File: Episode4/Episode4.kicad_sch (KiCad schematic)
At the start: 8 parts, among them J1 5V DC

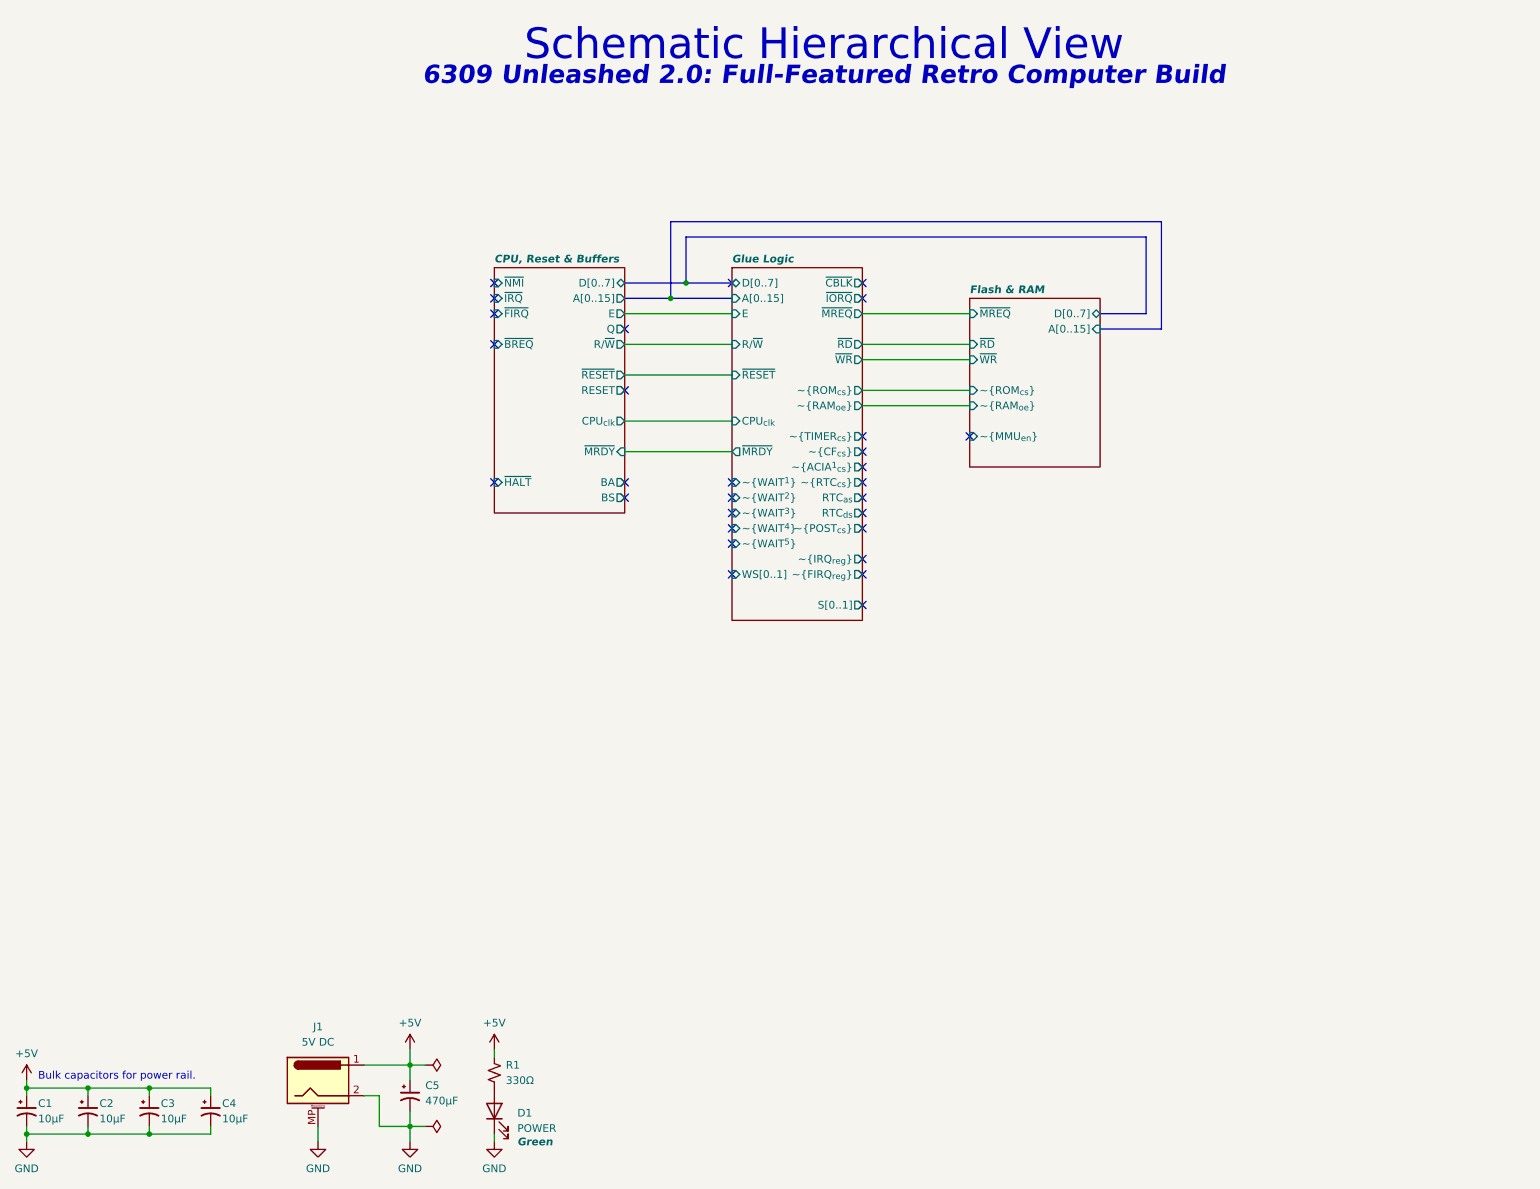
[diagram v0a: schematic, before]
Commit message: Project Update, change in strategy from breadboard to PCB
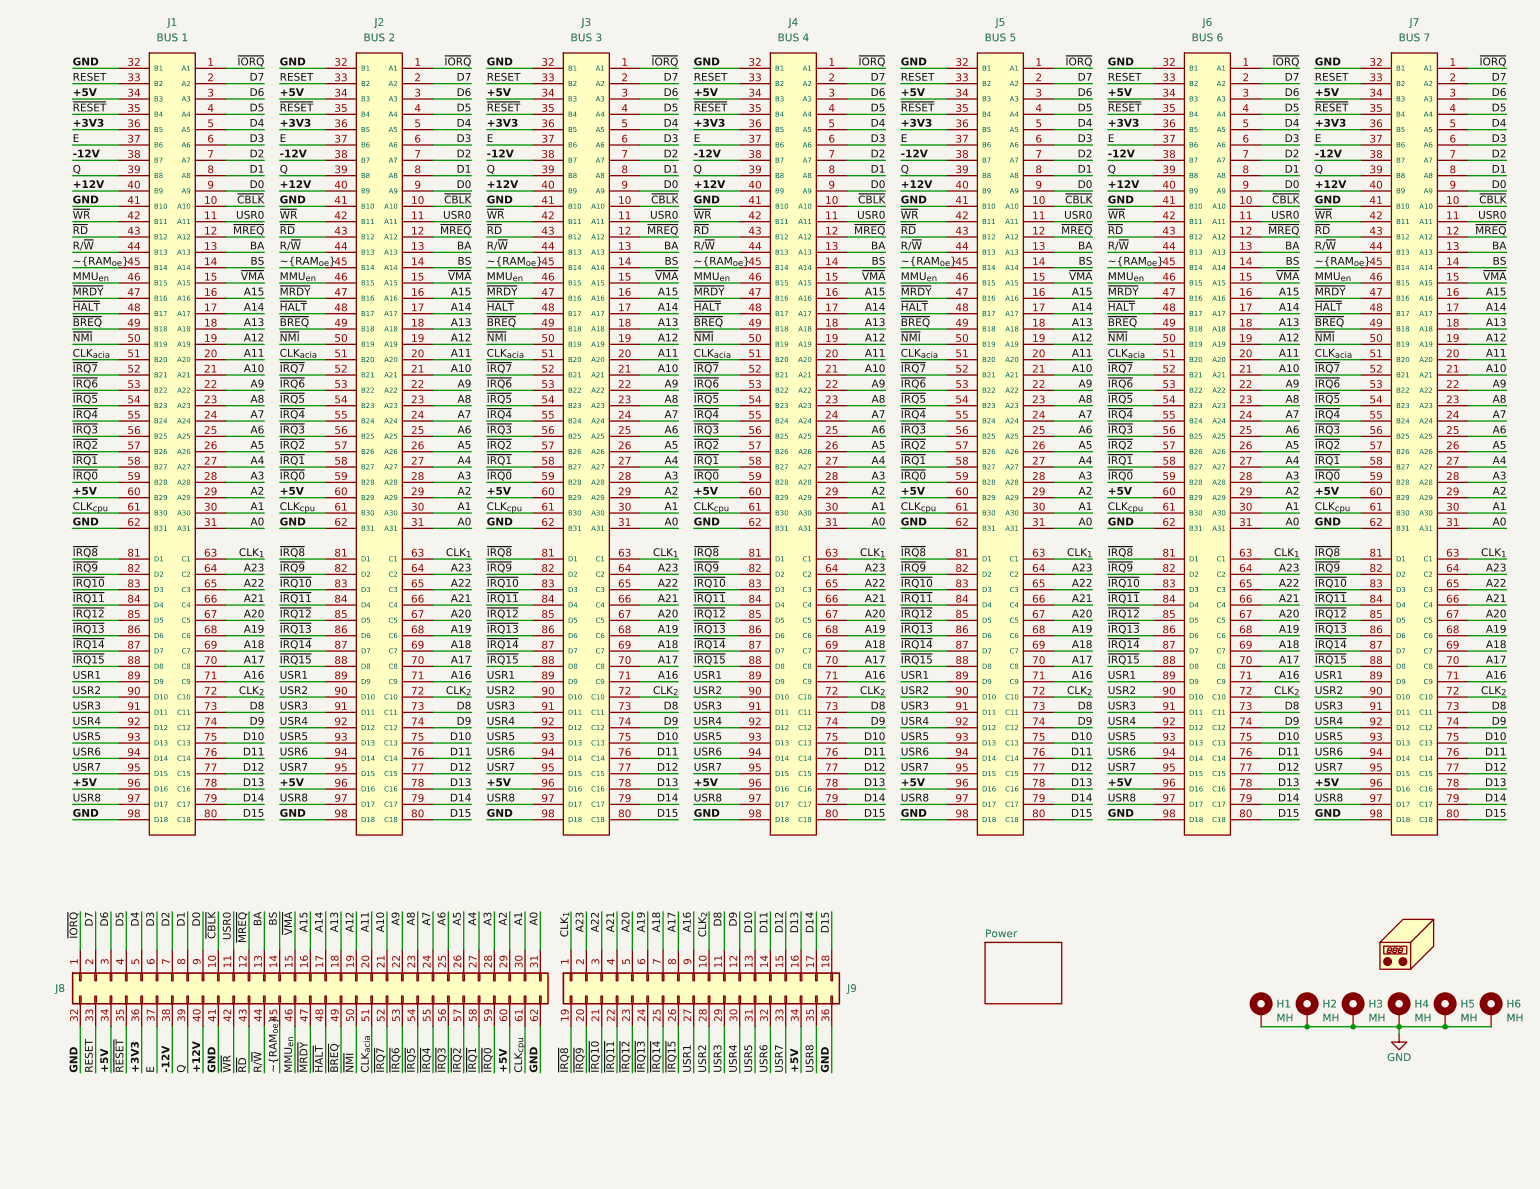
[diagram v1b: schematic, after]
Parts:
- removed C1, C2, C3, C4: 10µF, symbol Device:C_Polarized_Small_US
- removed C5: 470µF, symbol Device:C_Polarized_Small_US
- removed D1: POWER, symbol Device:LED
- removed J1: 5V DC, symbol Connector:Barrel_Jack_MountingPin
- removed R1: 330Ω, symbol Device:R_Small_US
- added H1, H2, H3, H4, H5, H6: MH, MountingHole:MountingHole_3.5mm_Pad_Via, symbol Mechanical:MountingHole_Pad
- added J1: BUS 1, MicroHobbyist:ISA_Connector_98, symbol MicroHobbyist:ISA_CARD_CONNECTOR_16BIT
- added J2: BUS 2, MicroHobbyist:ISA_Connector_98, symbol MicroHobbyist:ISA_CARD_CONNECTOR_16BIT
- added J3: BUS 3, MicroHobbyist:ISA_Connector_98, symbol MicroHobbyist:ISA_CARD_CONNECTOR_16BIT
- added J4: BUS 4, MicroHobbyist:ISA_Connector_98, symbol MicroHobbyist:ISA_CARD_CONNECTOR_16BIT
- added J5: BUS 5, MicroHobbyist:ISA_Connector_98, symbol MicroHobbyist:ISA_CARD_CONNECTOR_16BIT
- added J6: BUS 6, MicroHobbyist:ISA_Connector_98, symbol MicroHobbyist:ISA_CARD_CONNECTOR_16BIT
- added J7: BUS 7, MicroHobbyist:ISA_Connector_98, symbol MicroHobbyist:ISA_CARD_CONNECTOR_16BIT
- added J8: Conn_02x31_Top_Bottom, Connector_PinSocket_2.54mm:PinSocket_2x31_P2.54mm_Vertical, symbol Connector_Generic:Conn_02x31_Top_Bottom
- added J9: Conn_02x18_Top_Bottom, Connector_PinSocket_2.54mm:PinSocket_2x18_P2.54mm_Vertical, symbol Connector_Generic:Conn_02x18_Top_Bottom
- added N1: Housing, MicroHobbyist:ATX_Backplane, symbol Mechanical:Housing
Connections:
- net +5V: now also J1.34 (B3), J1.60 (B29), J1.96 (D16), J2.34 (B3), J2.60 (B29), J2.96 (D16), J3.34 (B3), J3.60 (B29), J3.96 (D16), J4.34 (B3), J4.60 (B29), J4.96 (D16), J5.34 (B3), J5.60 (B29), J5.96 (D16), J6.34 (B3), J6.60 (B29), J6.96 (D16), J7.34 (B3), J7.60 (B29), J7.96 (D16), J8.34 (Pin_34), J8.60 (Pin_60), J9.34 (Pin_34)
- net GND: now also H1.1, H2.1, H3.1, H4.1, H5.1, H6.1, J1.32 (B1), J1.41 (B10), J1.62 (B31), J1.98 (D18), J2.32 (B1), J2.41 (B10), J2.62 (B31), J2.98 (D18), J3.32 (B1), J3.41 (B10), J3.62 (B31), J3.98 (D18), J4.32 (B1), J4.41 (B10), J4.62 (B31), J4.98 (D18), J5.32 (B1), J5.41 (B10), J5.62 (B31), J5.98 (D18), J6.32 (B1), J6.41 (B10), J6.62 (B31), J6.98 (D18), J7.32 (B1), J7.41 (B10), J7.62 (B31), J7.98 (D18), J8.32 (Pin_32), J8.41 (Pin_41), J8.62 (Pin_62), J9.36 (Pin_36)
- new net +12V: J1.40 (B9), J2.40 (B9), J3.40 (B9), J4.40 (B9), J5.40 (B9), J6.40 (B9), J7.40 (B9), J8.40 (Pin_40)
- new net +3V3: J1.36 (B5), J2.36 (B5), J3.36 (B5), J4.36 (B5), J5.36 (B5), J6.36 (B5), J7.36 (B5), J8.36 (Pin_36)
- new net -12V: J1.38 (B7), J2.38 (B7), J3.38 (B7), J4.38 (B7), J5.38 (B7), J6.38 (B7), J7.38 (B7), J8.38 (Pin_38)
- new net A0: J1.31 (A31), J2.31 (A31), J3.31 (A31), J4.31 (A31), J5.31 (A31), J6.31 (A31), J7.31 (A31), J8.31 (Pin_31)
- new net A1: J1.30 (A30), J2.30 (A30), J3.30 (A30), J4.30 (A30), J5.30 (A30), J6.30 (A30), J7.30 (A30), J8.30 (Pin_30)
- new net A10: J1.21 (A21), J2.21 (A21), J3.21 (A21), J4.21 (A21), J5.21 (A21), J6.21 (A21), J7.21 (A21), J8.21 (Pin_21)
- new net A11: J1.20 (A20), J2.20 (A20), J3.20 (A20), J4.20 (A20), J5.20 (A20), J6.20 (A20), J7.20 (A20), J8.20 (Pin_20)
- new net A12: J1.19 (A19), J2.19 (A19), J3.19 (A19), J4.19 (A19), J5.19 (A19), J6.19 (A19), J7.19 (A19), J8.19 (Pin_19)
- new net A13: J1.18 (A18), J2.18 (A18), J3.18 (A18), J4.18 (A18), J5.18 (A18), J6.18 (A18), J7.18 (A18), J8.18 (Pin_18)
- new net A14: J1.17 (A17), J2.17 (A17), J3.17 (A17), J4.17 (A17), J5.17 (A17), J6.17 (A17), J7.17 (A17), J8.17 (Pin_17)
- new net A15: J1.16 (A16), J2.16 (A16), J3.16 (A16), J4.16 (A16), J5.16 (A16), J6.16 (A16), J7.16 (A16), J8.16 (Pin_16)
- new net A16: J1.71 (C9), J2.71 (C9), J3.71 (C9), J4.71 (C9), J5.71 (C9), J6.71 (C9), J7.71 (C9), J9.9 (Pin_9)
- new net A17: J1.70 (C8), J2.70 (C8), J3.70 (C8), J4.70 (C8), J5.70 (C8), J6.70 (C8), J7.70 (C8), J9.8 (Pin_8)
- new net A18: J1.69 (C7), J2.69 (C7), J3.69 (C7), J4.69 (C7), J5.69 (C7), J6.69 (C7), J7.69 (C7), J9.7 (Pin_7)
- new net A19: J1.68 (C6), J2.68 (C6), J3.68 (C6), J4.68 (C6), J5.68 (C6), J6.68 (C6), J7.68 (C6), J9.6 (Pin_6)
- new net A2: J1.29 (A29), J2.29 (A29), J3.29 (A29), J4.29 (A29), J5.29 (A29), J6.29 (A29), J7.29 (A29), J8.29 (Pin_29)
- new net A20: J1.67 (C5), J2.67 (C5), J3.67 (C5), J4.67 (C5), J5.67 (C5), J6.67 (C5), J7.67 (C5), J9.5 (Pin_5)
- new net A21: J1.66 (C4), J2.66 (C4), J3.66 (C4), J4.66 (C4), J5.66 (C4), J6.66 (C4), J7.66 (C4), J9.4 (Pin_4)
- new net A22: J1.65 (C3), J2.65 (C3), J3.65 (C3), J4.65 (C3), J5.65 (C3), J6.65 (C3), J7.65 (C3), J9.3 (Pin_3)
- new net A23: J1.64 (C2), J2.64 (C2), J3.64 (C2), J4.64 (C2), J5.64 (C2), J6.64 (C2), J7.64 (C2), J9.2 (Pin_2)
- new net A3: J1.28 (A28), J2.28 (A28), J3.28 (A28), J4.28 (A28), J5.28 (A28), J6.28 (A28), J7.28 (A28), J8.28 (Pin_28)
- new net A4: J1.27 (A27), J2.27 (A27), J3.27 (A27), J4.27 (A27), J5.27 (A27), J6.27 (A27), J7.27 (A27), J8.27 (Pin_27)
- new net A5: J1.26 (A26), J2.26 (A26), J3.26 (A26), J4.26 (A26), J5.26 (A26), J6.26 (A26), J7.26 (A26), J8.26 (Pin_26)
- new net A6: J1.25 (A25), J2.25 (A25), J3.25 (A25), J4.25 (A25), J5.25 (A25), J6.25 (A25), J7.25 (A25), J8.25 (Pin_25)
- new net A7: J1.24 (A24), J2.24 (A24), J3.24 (A24), J4.24 (A24), J5.24 (A24), J6.24 (A24), J7.24 (A24), J8.24 (Pin_24)
- new net A8: J1.23 (A23), J2.23 (A23), J3.23 (A23), J4.23 (A23), J5.23 (A23), J6.23 (A23), J7.23 (A23), J8.23 (Pin_23)
- new net A9: J1.22 (A22), J2.22 (A22), J3.22 (A22), J4.22 (A22), J5.22 (A22), J6.22 (A22), J7.22 (A22), J8.22 (Pin_22)
- new net BA: J1.13 (A13), J2.13 (A13), J3.13 (A13), J4.13 (A13), J5.13 (A13), J6.13 (A13), J7.13 (A13), J8.13 (Pin_13)
- new net BS: J1.14 (A14), J2.14 (A14), J3.14 (A14), J4.14 (A14), J5.14 (A14), J6.14 (A14), J7.14 (A14), J8.14 (Pin_14)
- new net CLK_{1}: J1.63 (C1), J2.63 (C1), J3.63 (C1), J4.63 (C1), J5.63 (C1), J6.63 (C1), J7.63 (C1), J9.1 (Pin_1)
- new net CLK_{2}: J1.72 (C10), J2.72 (C10), J3.72 (C10), J4.72 (C10), J5.72 (C10), J6.72 (C10), J7.72 (C10), J9.10 (Pin_10)
- new net CLK_{acia}: J1.51 (B20), J2.51 (B20), J3.51 (B20), J4.51 (B20), J5.51 (B20), J6.51 (B20), J7.51 (B20), J8.51 (Pin_51)
- new net CLK_{cpu}: J1.61 (B30), J2.61 (B30), J3.61 (B30), J4.61 (B30), J5.61 (B30), J6.61 (B30), J7.61 (B30), J8.61 (Pin_61)
- new net D0: J1.9 (A9), J2.9 (A9), J3.9 (A9), J4.9 (A9), J5.9 (A9), J6.9 (A9), J7.9 (A9), J8.9 (Pin_9)
- new net D1: J1.8 (A8), J2.8 (A8), J3.8 (A8), J4.8 (A8), J5.8 (A8), J6.8 (A8), J7.8 (A8), J8.8 (Pin_8)
- new net D10: J1.75 (C13), J2.75 (C13), J3.75 (C13), J4.75 (C13), J5.75 (C13), J6.75 (C13), J7.75 (C13), J9.13 (Pin_13)
- new net D11: J1.76 (C14), J2.76 (C14), J3.76 (C14), J4.76 (C14), J5.76 (C14), J6.76 (C14), J7.76 (C14), J9.14 (Pin_14)
- new net D12: J1.77 (C15), J2.77 (C15), J3.77 (C15), J4.77 (C15), J5.77 (C15), J6.77 (C15), J7.77 (C15), J9.15 (Pin_15)
- new net D13: J1.78 (C16), J2.78 (C16), J3.78 (C16), J4.78 (C16), J5.78 (C16), J6.78 (C16), J7.78 (C16), J9.16 (Pin_16)
- new net D14: J1.79 (C17), J2.79 (C17), J3.79 (C17), J4.79 (C17), J5.79 (C17), J6.79 (C17), J7.79 (C17), J9.17 (Pin_17)
- new net D15: J1.80 (C18), J2.80 (C18), J3.80 (C18), J4.80 (C18), J5.80 (C18), J6.80 (C18), J7.80 (C18), J9.18 (Pin_18)
- new net D2: J1.7 (A7), J2.7 (A7), J3.7 (A7), J4.7 (A7), J5.7 (A7), J6.7 (A7), J7.7 (A7), J8.7 (Pin_7)
- new net D3: J1.6 (A6), J2.6 (A6), J3.6 (A6), J4.6 (A6), J5.6 (A6), J6.6 (A6), J7.6 (A6), J8.6 (Pin_6)
- new net D4: J1.5 (A5), J2.5 (A5), J3.5 (A5), J4.5 (A5), J5.5 (A5), J6.5 (A5), J7.5 (A5), J8.5 (Pin_5)
- new net D5: J1.4 (A4), J2.4 (A4), J3.4 (A4), J4.4 (A4), J5.4 (A4), J6.4 (A4), J7.4 (A4), J8.4 (Pin_4)
- new net D6: J1.3 (A3), J2.3 (A3), J3.3 (A3), J4.3 (A3), J5.3 (A3), J6.3 (A3), J7.3 (A3), J8.3 (Pin_3)
- new net D7: J1.2 (A2), J2.2 (A2), J3.2 (A2), J4.2 (A2), J5.2 (A2), J6.2 (A2), J7.2 (A2), J8.2 (Pin_2)
- new net D8: J1.73 (C11), J2.73 (C11), J3.73 (C11), J4.73 (C11), J5.73 (C11), J6.73 (C11), J7.73 (C11), J9.11 (Pin_11)
- new net D9: J1.74 (C12), J2.74 (C12), J3.74 (C12), J4.74 (C12), J5.74 (C12), J6.74 (C12), J7.74 (C12), J9.12 (Pin_12)
- new net E: J1.37 (B6), J2.37 (B6), J3.37 (B6), J4.37 (B6), J5.37 (B6), J6.37 (B6), J7.37 (B6), J8.37 (Pin_37)
- new net MMU_{en}: J1.46 (B15), J2.46 (B15), J3.46 (B15), J4.46 (B15), J5.46 (B15), J6.46 (B15), J7.46 (B15), J8.46 (Pin_46)
- new net Q: J1.39 (B8), J2.39 (B8), J3.39 (B8), J4.39 (B8), J5.39 (B8), J6.39 (B8), J7.39 (B8), J8.39 (Pin_39)
- new net RESET: J1.33 (B2), J2.33 (B2), J3.33 (B2), J4.33 (B2), J5.33 (B2), J6.33 (B2), J7.33 (B2), J8.33 (Pin_33)
- new net R/~{W}: J1.44 (B13), J2.44 (B13), J3.44 (B13), J4.44 (B13), J5.44 (B13), J6.44 (B13), J7.44 (B13), J8.44 (Pin_44)
- new net USR0: J1.11 (A11), J2.11 (A11), J3.11 (A11), J4.11 (A11), J5.11 (A11), J6.11 (A11), J7.11 (A11), J8.11 (Pin_11)
- new net USR1: J1.89 (D9), J2.89 (D9), J3.89 (D9), J4.89 (D9), J5.89 (D9), J6.89 (D9), J7.89 (D9), J9.27 (Pin_27)
- new net USR2: J1.90 (D10), J2.90 (D10), J3.90 (D10), J4.90 (D10), J5.90 (D10), J6.90 (D10), J7.90 (D10), J9.28 (Pin_28)
- new net USR3: J1.91 (D11), J2.91 (D11), J3.91 (D11), J4.91 (D11), J5.91 (D11), J6.91 (D11), J7.91 (D11), J9.29 (Pin_29)
- new net USR4: J1.92 (D12), J2.92 (D12), J3.92 (D12), J4.92 (D12), J5.92 (D12), J6.92 (D12), J7.92 (D12), J9.30 (Pin_30)
- new net USR5: J1.93 (D13), J2.93 (D13), J3.93 (D13), J4.93 (D13), J5.93 (D13), J6.93 (D13), J7.93 (D13), J9.31 (Pin_31)
- new net USR6: J1.94 (D14), J2.94 (D14), J3.94 (D14), J4.94 (D14), J5.94 (D14), J6.94 (D14), J7.94 (D14), J9.32 (Pin_32)
- new net USR7: J1.95 (D15), J2.95 (D15), J3.95 (D15), J4.95 (D15), J5.95 (D15), J6.95 (D15), J7.95 (D15), J9.33 (Pin_33)
- new net USR8: J1.97 (D17), J2.97 (D17), J3.97 (D17), J4.97 (D17), J5.97 (D17), J6.97 (D17), J7.97 (D17), J9.35 (Pin_35)
- new net ~{BREQ}: J1.49 (B18), J2.49 (B18), J3.49 (B18), J4.49 (B18), J5.49 (B18), J6.49 (B18), J7.49 (B18), J8.49 (Pin_49)
- new net ~{CBLK}: J1.10 (A10), J2.10 (A10), J3.10 (A10), J4.10 (A10), J5.10 (A10), J6.10 (A10), J7.10 (A10), J8.10 (Pin_10)
- new net ~{HALT}: J1.48 (B17), J2.48 (B17), J3.48 (B17), J4.48 (B17), J5.48 (B17), J6.48 (B17), J7.48 (B17), J8.48 (Pin_48)
- new net ~{IORQ}: J1.1 (A1), J2.1 (A1), J3.1 (A1), J4.1 (A1), J5.1 (A1), J6.1 (A1), J7.1 (A1), J8.1 (Pin_1)
- new net ~{IRQ0}: J1.59 (B28), J2.59 (B28), J3.59 (B28), J4.59 (B28), J5.59 (B28), J6.59 (B28), J7.59 (B28), J8.59 (Pin_59)
- new net ~{IRQ10}: J1.83 (D3), J2.83 (D3), J3.83 (D3), J4.83 (D3), J5.83 (D3), J6.83 (D3), J7.83 (D3), J9.21 (Pin_21)
- new net ~{IRQ11}: J1.84 (D4), J2.84 (D4), J3.84 (D4), J4.84 (D4), J5.84 (D4), J6.84 (D4), J7.84 (D4), J9.22 (Pin_22)
- new net ~{IRQ12}: J1.85 (D5), J2.85 (D5), J3.85 (D5), J4.85 (D5), J5.85 (D5), J6.85 (D5), J7.85 (D5), J9.23 (Pin_23)
- new net ~{IRQ13}: J1.86 (D6), J2.86 (D6), J3.86 (D6), J4.86 (D6), J5.86 (D6), J6.86 (D6), J7.86 (D6), J9.24 (Pin_24)
- new net ~{IRQ14}: J1.87 (D7), J2.87 (D7), J3.87 (D7), J4.87 (D7), J5.87 (D7), J6.87 (D7), J7.87 (D7), J9.25 (Pin_25)
- new net ~{IRQ15}: J1.88 (D8), J2.88 (D8), J3.88 (D8), J4.88 (D8), J5.88 (D8), J6.88 (D8), J7.88 (D8), J9.26 (Pin_26)
- new net ~{IRQ1}: J1.58 (B27), J2.58 (B27), J3.58 (B27), J4.58 (B27), J5.58 (B27), J6.58 (B27), J7.58 (B27), J8.58 (Pin_58)
- new net ~{IRQ2}: J1.57 (B26), J2.57 (B26), J3.57 (B26), J4.57 (B26), J5.57 (B26), J6.57 (B26), J7.57 (B26), J8.57 (Pin_57)
- new net ~{IRQ3}: J1.56 (B25), J2.56 (B25), J3.56 (B25), J4.56 (B25), J5.56 (B25), J6.56 (B25), J7.56 (B25), J8.56 (Pin_56)
- new net ~{IRQ4}: J1.55 (B24), J2.55 (B24), J3.55 (B24), J4.55 (B24), J5.55 (B24), J6.55 (B24), J7.55 (B24), J8.55 (Pin_55)
- new net ~{IRQ5}: J1.54 (B23), J2.54 (B23), J3.54 (B23), J4.54 (B23), J5.54 (B23), J6.54 (B23), J7.54 (B23), J8.54 (Pin_54)
- new net ~{IRQ6}: J1.53 (B22), J2.53 (B22), J3.53 (B22), J4.53 (B22), J5.53 (B22), J6.53 (B22), J7.53 (B22), J8.53 (Pin_53)
- new net ~{IRQ7}: J1.52 (B21), J2.52 (B21), J3.52 (B21), J4.52 (B21), J5.52 (B21), J6.52 (B21), J7.52 (B21), J8.52 (Pin_52)
- new net ~{IRQ8}: J1.81 (D1), J2.81 (D1), J3.81 (D1), J4.81 (D1), J5.81 (D1), J6.81 (D1), J7.81 (D1), J9.19 (Pin_19)
- new net ~{IRQ9}: J1.82 (D2), J2.82 (D2), J3.82 (D2), J4.82 (D2), J5.82 (D2), J6.82 (D2), J7.82 (D2), J9.20 (Pin_20)
- new net ~{MRDY}: J1.47 (B16), J2.47 (B16), J3.47 (B16), J4.47 (B16), J5.47 (B16), J6.47 (B16), J7.47 (B16), J8.47 (Pin_47)
- new net ~{MREQ}: J1.12 (A12), J2.12 (A12), J3.12 (A12), J4.12 (A12), J5.12 (A12), J6.12 (A12), J7.12 (A12), J8.12 (Pin_12)
- new net ~{NMI}: J1.50 (B19), J2.50 (B19), J3.50 (B19), J4.50 (B19), J5.50 (B19), J6.50 (B19), J7.50 (B19), J8.50 (Pin_50)
- new net ~{RAM_{oe}}: J1.45 (B14), J2.45 (B14), J3.45 (B14), J4.45 (B14), J5.45 (B14), J6.45 (B14), J7.45 (B14), J8.45 (Pin_45)
- new net ~{RD}: J1.43 (B12), J2.43 (B12), J3.43 (B12), J4.43 (B12), J5.43 (B12), J6.43 (B12), J7.43 (B12), J8.43 (Pin_43)
- new net ~{RESET}: J1.35 (B4), J2.35 (B4), J3.35 (B4), J4.35 (B4), J5.35 (B4), J6.35 (B4), J7.35 (B4), J8.35 (Pin_35)
- new net ~{VMA}: J1.15 (A15), J2.15 (A15), J3.15 (A15), J4.15 (A15), J5.15 (A15), J6.15 (A15), J7.15 (A15), J8.15 (Pin_15)
- new net ~{WR}: J1.42 (B11), J2.42 (B11), J3.42 (B11), J4.42 (B11), J5.42 (B11), J6.42 (B11), J7.42 (B11), J8.42 (Pin_42)
- no-connect marks 29 -> 0
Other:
- removed sheet CPU, Reset & Buffers
- removed sheet Flash & RAM
- removed sheet Glue Logic
- added sheet Power (SoftPower.kicad_sch)
- note removed: "6309 Unleashed 2.0: Full-Featured Retro Computer Build"
- note removed: "Bulk capacitors for power rail."
- note removed: "Schematic Hierarchical View"
- title: 6309 Full-Featured Computer -> 16-bit ATX backblane

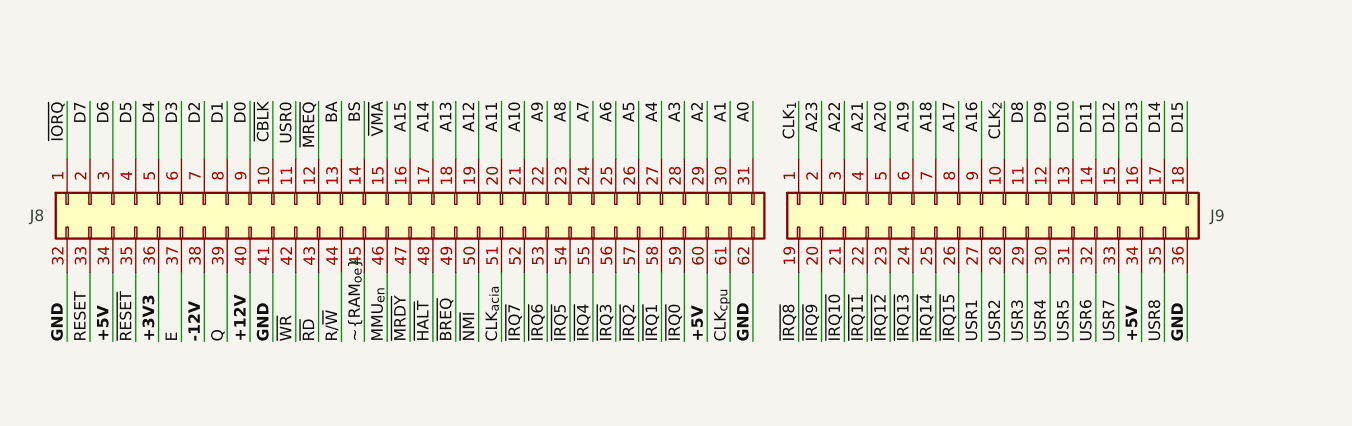
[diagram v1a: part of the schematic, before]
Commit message: Added traces to the backplane manually.
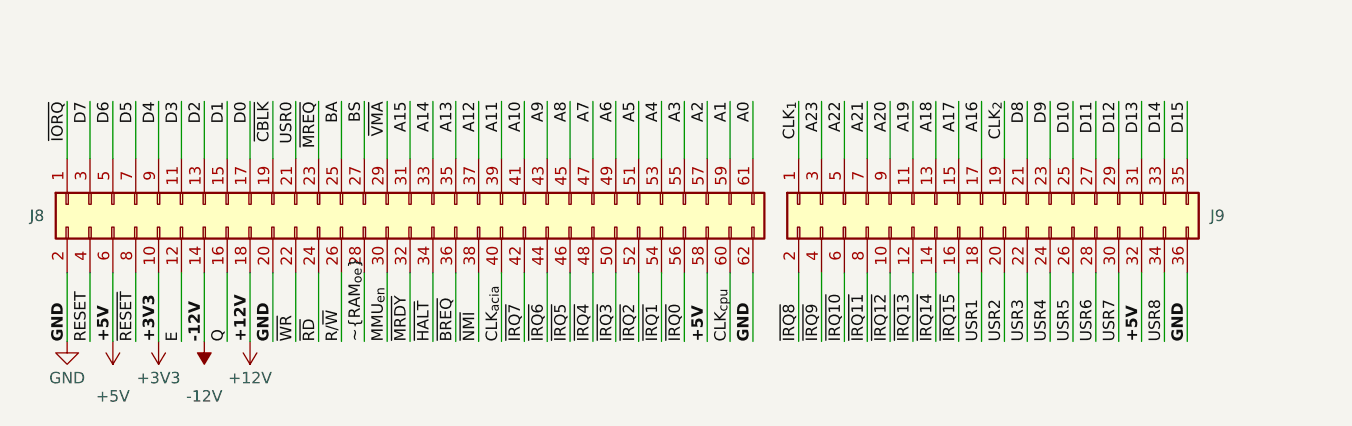
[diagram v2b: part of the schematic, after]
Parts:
- J8: symbol Connector_Generic:Conn_02x31_Top_Bottom -> Connector_Generic:Conn_02x31_Odd_Even
- J9: symbol Connector_Generic:Conn_02x18_Top_Bottom -> Connector_Generic:Conn_02x18_Odd_Even
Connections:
- net +12V: now also J8.18 (Pin_18); no longer J8.40 (Pin_40)
- net +3V3: now also J8.10 (Pin_10); no longer J8.36 (Pin_36)
- net +5V: now also J8.58 (Pin_58), J8.6 (Pin_6), J9.32 (Pin_32); no longer J8.34 (Pin_34), J8.60 (Pin_60), J9.34 (Pin_34)
- net -12V: now also J8.14 (Pin_14); no longer J8.38 (Pin_38)
- net A0: now also J8.61 (Pin_61); no longer J8.31 (Pin_31)
- net A1: now also J8.59 (Pin_59); no longer J8.30 (Pin_30)
- net A10: now also J8.41 (Pin_41); no longer J8.21 (Pin_21)
- net A11: now also J8.39 (Pin_39); no longer J8.20 (Pin_20)
- net A12: now also J8.37 (Pin_37); no longer J8.19 (Pin_19)
- net A13: now also J8.35 (Pin_35); no longer J8.18 (Pin_18)
- net A14: now also J8.33 (Pin_33); no longer J8.17 (Pin_17)
- net A15: now also J8.31 (Pin_31); no longer J8.16 (Pin_16)
- net A16: now also J9.17 (Pin_17); no longer J9.9 (Pin_9)
- net A17: now also J9.15 (Pin_15); no longer J9.8 (Pin_8)
- net A18: now also J9.13 (Pin_13); no longer J9.7 (Pin_7)
- net A19: now also J9.11 (Pin_11); no longer J9.6 (Pin_6)
- net A2: now also J8.57 (Pin_57); no longer J8.29 (Pin_29)
- net A20: now also J9.9 (Pin_9); no longer J9.5 (Pin_5)
- net A21: now also J9.7 (Pin_7); no longer J9.4 (Pin_4)
- net A22: now also J9.5 (Pin_5); no longer J9.3 (Pin_3)
- net A23: now also J9.3 (Pin_3); no longer J9.2 (Pin_2)
- net A3: now also J8.55 (Pin_55); no longer J8.28 (Pin_28)
- net A4: now also J8.53 (Pin_53); no longer J8.27 (Pin_27)
- net A5: now also J8.51 (Pin_51); no longer J8.26 (Pin_26)
- net A6: now also J8.49 (Pin_49); no longer J8.25 (Pin_25)
- net A7: now also J8.47 (Pin_47); no longer J8.24 (Pin_24)
- net A8: now also J8.45 (Pin_45); no longer J8.23 (Pin_23)
- net A9: now also J8.43 (Pin_43); no longer J8.22 (Pin_22)
- net BA: now also J8.25 (Pin_25); no longer J8.13 (Pin_13)
- net BS: now also J8.27 (Pin_27); no longer J8.14 (Pin_14)
- net CLK_{2}: now also J9.19 (Pin_19); no longer J9.10 (Pin_10)
- net CLK_{acia}: now also J8.40 (Pin_40); no longer J8.51 (Pin_51)
- net CLK_{cpu}: now also J8.60 (Pin_60); no longer J8.61 (Pin_61)
- net D0: now also J8.17 (Pin_17); no longer J8.9 (Pin_9)
- net D1: now also J8.15 (Pin_15); no longer J8.8 (Pin_8)
- net D10: now also J9.25 (Pin_25); no longer J9.13 (Pin_13)
- net D11: now also J9.27 (Pin_27); no longer J9.14 (Pin_14)
- net D12: now also J9.29 (Pin_29); no longer J9.15 (Pin_15)
- net D13: now also J9.31 (Pin_31); no longer J9.16 (Pin_16)
- net D14: now also J9.33 (Pin_33); no longer J9.17 (Pin_17)
- net D15: now also J9.35 (Pin_35); no longer J9.18 (Pin_18)
- net D2: now also J8.13 (Pin_13); no longer J8.7 (Pin_7)
- net D3: now also J8.11 (Pin_11); no longer J8.6 (Pin_6)
- net D4: now also J8.9 (Pin_9); no longer J8.5 (Pin_5)
- net D5: now also J8.7 (Pin_7); no longer J8.4 (Pin_4)
- net D6: now also J8.5 (Pin_5); no longer J8.3 (Pin_3)
- net D7: now also J8.3 (Pin_3); no longer J8.2 (Pin_2)
- net D8: now also J9.21 (Pin_21); no longer J9.11 (Pin_11)
- net D9: now also J9.23 (Pin_23); no longer J9.12 (Pin_12)
- net E: now also J8.12 (Pin_12); no longer J8.37 (Pin_37)
- net GND: now also J8.2 (Pin_2), J8.20 (Pin_20); no longer J8.32 (Pin_32), J8.41 (Pin_41)
- net MMU_{en}: now also J8.30 (Pin_30); no longer J8.46 (Pin_46)
- net Q: now also J8.16 (Pin_16); no longer J8.39 (Pin_39)
- net RESET: now also J8.4 (Pin_4); no longer J8.33 (Pin_33)
- net R/~{W}: now also J8.26 (Pin_26); no longer J8.44 (Pin_44)
- net USR0: now also J8.21 (Pin_21); no longer J8.11 (Pin_11)
- net USR1: now also J9.18 (Pin_18); no longer J9.27 (Pin_27)
- net USR2: now also J9.20 (Pin_20); no longer J9.28 (Pin_28)
- net USR3: now also J9.22 (Pin_22); no longer J9.29 (Pin_29)
- net USR4: now also J9.24 (Pin_24); no longer J9.30 (Pin_30)
- net USR5: now also J9.26 (Pin_26); no longer J9.31 (Pin_31)
- net USR6: now also J9.28 (Pin_28); no longer J9.32 (Pin_32)
- net USR7: now also J9.30 (Pin_30); no longer J9.33 (Pin_33)
- net USR8: now also J9.34 (Pin_34); no longer J9.35 (Pin_35)
- net ~{BREQ}: now also J8.36 (Pin_36); no longer J8.49 (Pin_49)
- net ~{CBLK}: now also J8.19 (Pin_19); no longer J8.10 (Pin_10)
- net ~{HALT}: now also J8.34 (Pin_34); no longer J8.48 (Pin_48)
- net ~{IRQ0}: now also J8.56 (Pin_56); no longer J8.59 (Pin_59)
- net ~{IRQ10}: now also J9.6 (Pin_6); no longer J9.21 (Pin_21)
- net ~{IRQ11}: now also J9.8 (Pin_8); no longer J9.22 (Pin_22)
- net ~{IRQ12}: now also J9.10 (Pin_10); no longer J9.23 (Pin_23)
- net ~{IRQ13}: now also J9.12 (Pin_12); no longer J9.24 (Pin_24)
- net ~{IRQ14}: now also J9.14 (Pin_14); no longer J9.25 (Pin_25)
- net ~{IRQ15}: now also J9.16 (Pin_16); no longer J9.26 (Pin_26)
- net ~{IRQ1}: now also J8.54 (Pin_54); no longer J8.58 (Pin_58)
- net ~{IRQ2}: now also J8.52 (Pin_52); no longer J8.57 (Pin_57)
- net ~{IRQ3}: now also J8.50 (Pin_50); no longer J8.56 (Pin_56)
- net ~{IRQ4}: now also J8.48 (Pin_48); no longer J8.55 (Pin_55)
- net ~{IRQ5}: now also J8.46 (Pin_46); no longer J8.54 (Pin_54)
- net ~{IRQ6}: now also J8.44 (Pin_44); no longer J8.53 (Pin_53)
- net ~{IRQ7}: now also J8.42 (Pin_42); no longer J8.52 (Pin_52)
- net ~{IRQ8}: now also J9.2 (Pin_2); no longer J9.19 (Pin_19)
- net ~{IRQ9}: now also J9.4 (Pin_4); no longer J9.20 (Pin_20)
- net ~{MRDY}: now also J8.32 (Pin_32); no longer J8.47 (Pin_47)
- net ~{MREQ}: now also J8.23 (Pin_23); no longer J8.12 (Pin_12)
- net ~{NMI}: now also J8.38 (Pin_38); no longer J8.50 (Pin_50)
- net ~{RAM_{oe}}: now also J8.28 (Pin_28); no longer J8.45 (Pin_45)
- net ~{RD}: now also J8.24 (Pin_24); no longer J8.43 (Pin_43)
- net ~{RESET}: now also J8.8 (Pin_8); no longer J8.35 (Pin_35)
- net ~{VMA}: now also J8.29 (Pin_29); no longer J8.15 (Pin_15)
- net ~{WR}: now also J8.22 (Pin_22); no longer J8.42 (Pin_42)
